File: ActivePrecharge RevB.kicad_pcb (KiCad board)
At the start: 2 copper layers, 98.4 x 58.9 mm, 93 parts, among them IC1 AMC1350DWVR, IC2 AMC1350DWVR, IC3 ZXRE160AET5TA, J1 HVConnector, J2 ExportConnector, J3 PrechargeContactor, J4 MainContactor, U1 LT1963AEST-3.3#TRPBF, U2 TLV9001IDBVR, U3 TLV9001IDBVR

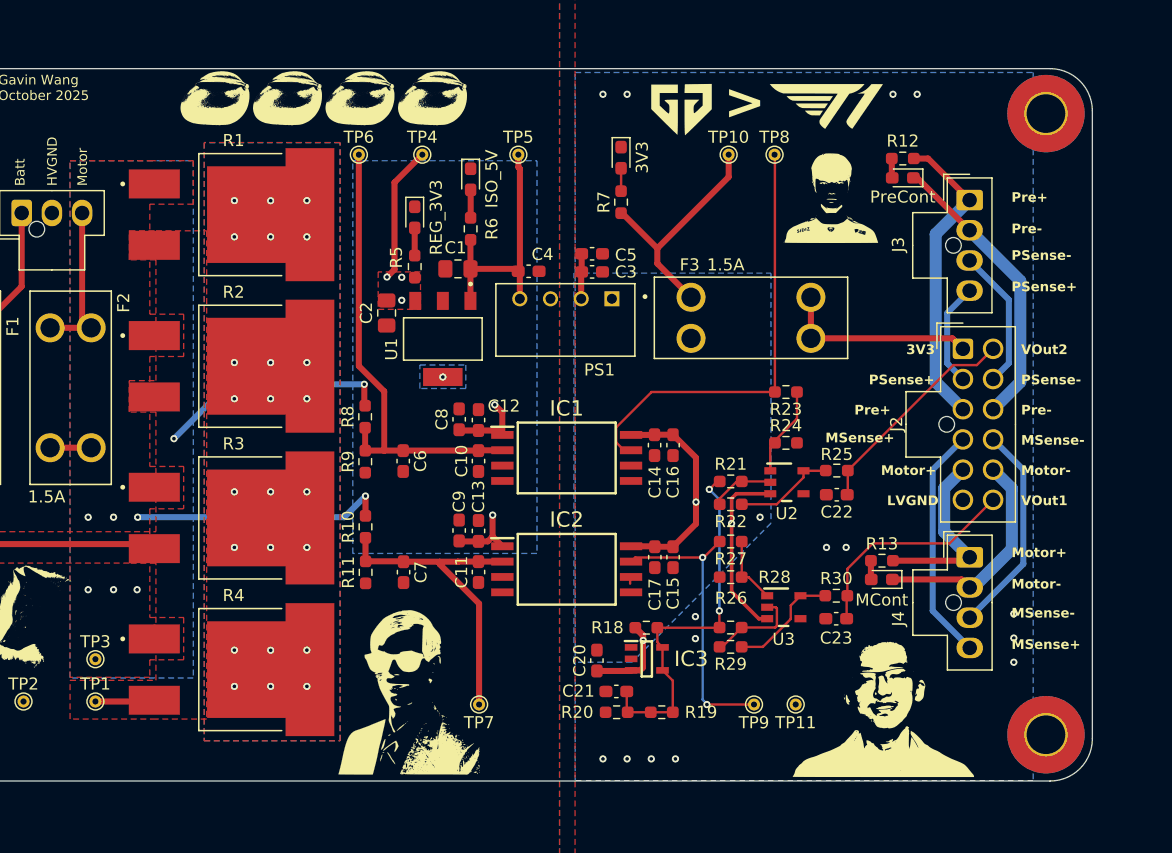
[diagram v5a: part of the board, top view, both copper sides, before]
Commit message: Renamed connector pins and added stitching vias for LVGND island
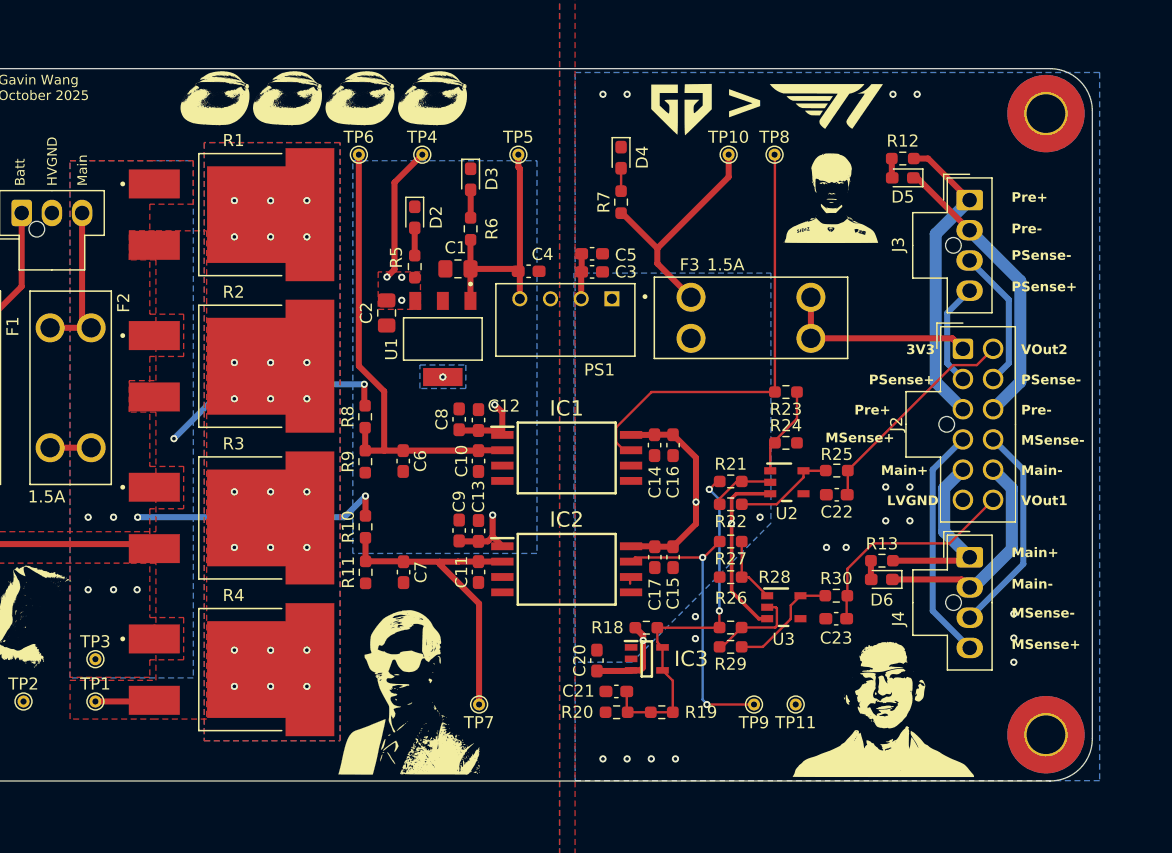
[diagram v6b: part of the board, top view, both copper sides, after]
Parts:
- renumbered REG_3V3 to D2, ISO_5V to D3, 3V3 to D4, PreCont to D5, MCont to D6
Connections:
- net /Motor+ renamed /Main+
- net /Motor- renamed /Main-
- net /MotorSense+ renamed /MainSense+
- net /MotorSense- renamed /MainSense-
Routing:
- net LVGND: vias 17 -> 21
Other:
- board text added: "Main"
- board text added: "Main+"
- board text added: "Main-"
- board text removed: "Motor"
- board text removed: "Motor+"
- board text removed: "Motor-"
